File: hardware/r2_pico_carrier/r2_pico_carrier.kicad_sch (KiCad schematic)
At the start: 67 parts, among them J1 5V in, J2 OLED socket, SW1 display, U1 PCA9517A

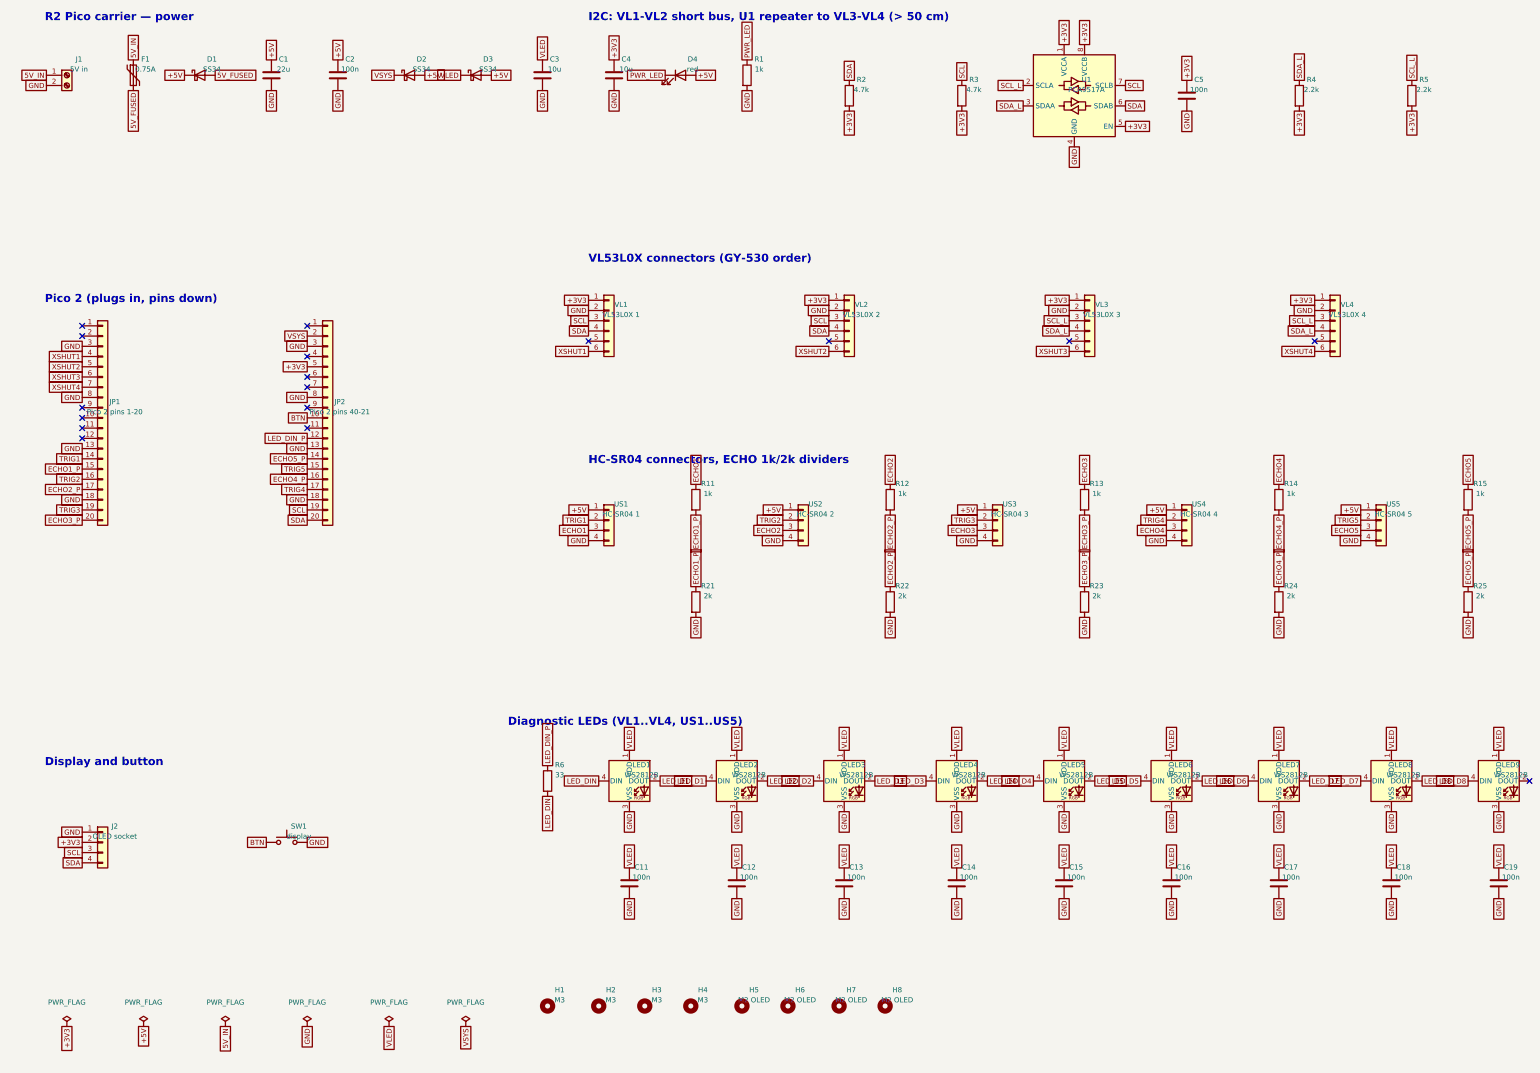
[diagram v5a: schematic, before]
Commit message: Carrier board: plain 0603 status LEDs, one GPIO each (VL1-4 = GP28/27/22/9, US1-5 = GP0/1/6-8), in place of the WS2812B chain; no VLED rail; BOM 17 lines
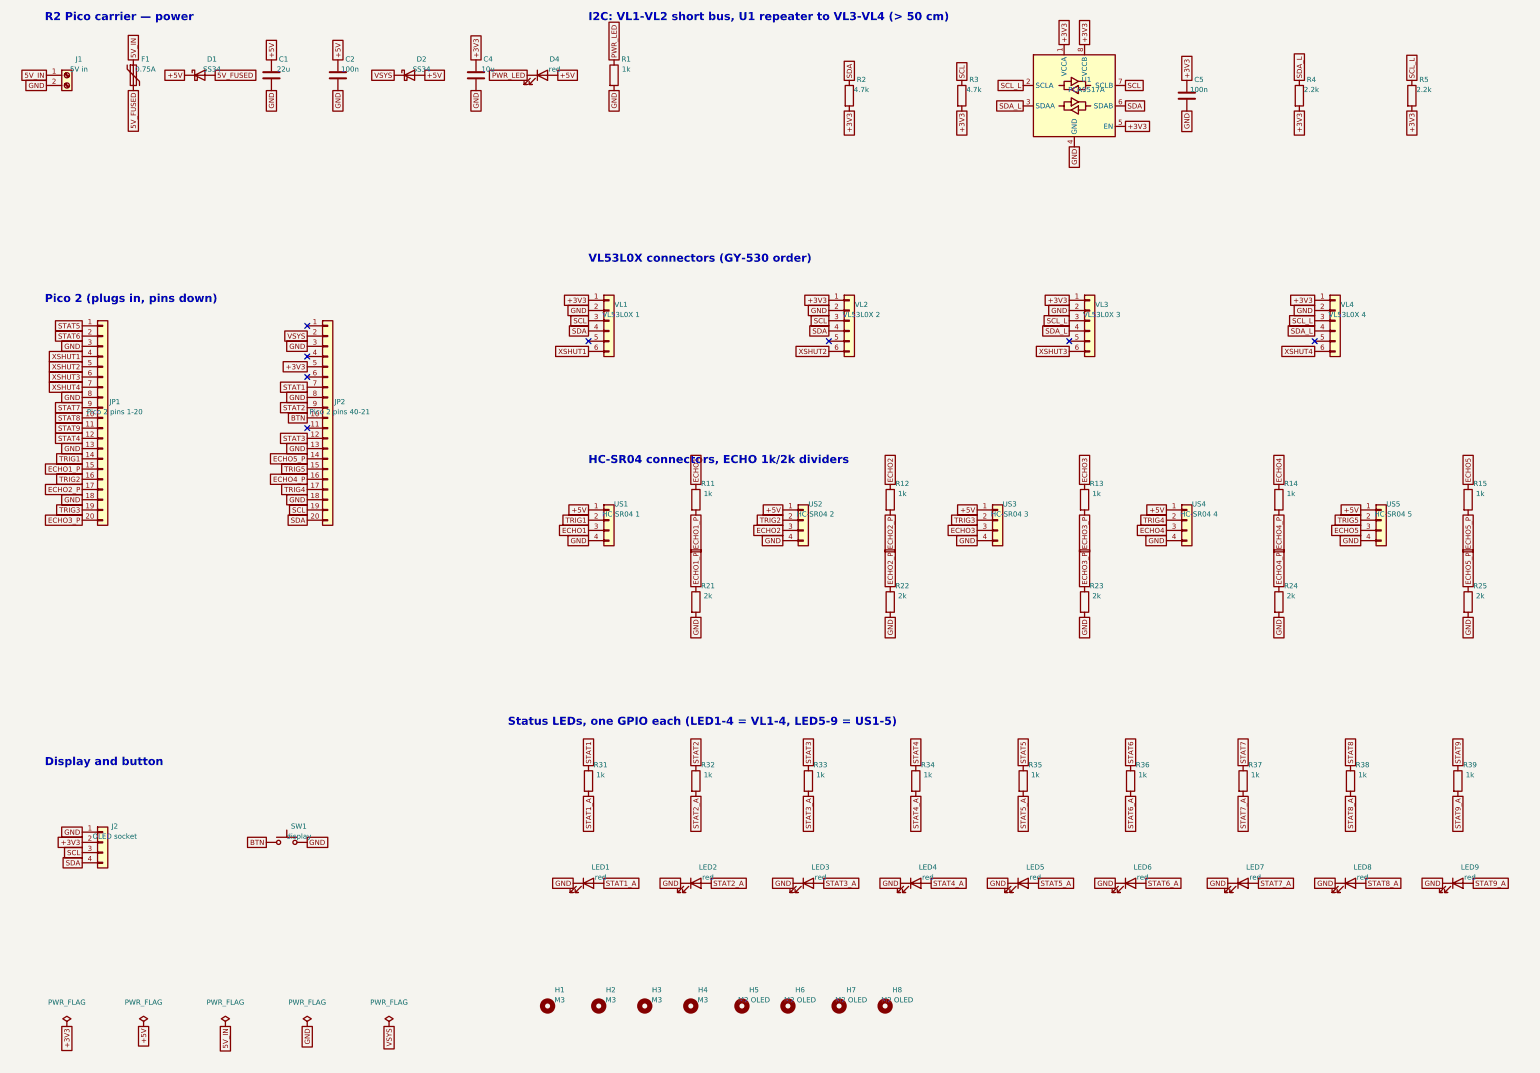
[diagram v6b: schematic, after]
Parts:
- removed C11, C12, C13, C14, C15, C16, C17, C18, C19: 100n, Capacitor_SMD:C_0603_1608Metric, symbol Device:C
- removed C3: 10u, Capacitor_SMD:C_0805_2012Metric, symbol Device:C
- removed D3: SS34, Diode_SMD:D_SMA, symbol Device:D_Schottky
- removed R6: 33, Resistor_SMD:R_0603_1608Metric, symbol Device:R
- added R31, R32, R33, R34, R35, R36, R37, R38, R39: 1k, Resistor_SMD:R_0603_1608Metric, symbol Device:R
- LED1, LED2, LED3, LED4, LED5, LED6, LED7, LED8, LED9: value WS2812B -> red; footprint LED_SMD:LED_WS2812B_PLCC4_5.0x5.0mm_P3.2mm -> LED_SMD:LED_0603_1608Metric; symbol LED:WS2812B -> Device:LED; LCSC C2874885 -> C2286
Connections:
- net VLED is gone; now on net GND: LED1.1 (K), LED2.1 (K), LED3.1 (K), LED4.1 (K), LED5.1 (K), LED6.1 (K), LED7.1 (K), LED8.1 (K), LED9.1 (K)
- net GND: no longer LED1.3 (VSS), LED2.3 (VSS), LED3.3 (VSS), LED4.3 (VSS), LED5.3 (VSS), LED6.3 (VSS), LED7.3 (VSS), LED8.3 (VSS), LED9.3 (VSS)
- net STAT9_A: now reaches LED9.2 (A)
- net STAT9_A: now also R39.2
- net STAT5: now reaches JP1.1 (Pin_1)
- net STAT5: now also R35.1
- net STAT8: now reaches JP1.10 (Pin_10)
- net STAT8: now also R38.1
- net STAT9: now reaches JP1.11 (Pin_11)
- net STAT9: now also R39.1
- net STAT4: now reaches JP1.12 (Pin_12)
- net STAT4: now also R34.1
- net STAT6: now reaches JP1.2 (Pin_2)
- net STAT6: now also R36.1
- net STAT7: now reaches JP1.9 (Pin_9)
- net STAT7: now also R37.1
- net STAT1: now reaches JP2.7 (Pin_7)
- net STAT1: now also R31.1
- net STAT2: now reaches JP2.9 (Pin_9)
- net STAT2: now also R32.1
- net LED_D1 renamed STAT1_A
- net STAT1_A: now also R31.2; no longer LED2.4 (DIN)
- net LED_D2 renamed STAT2_A
- net STAT2_A: now also R32.2; no longer LED3.4 (DIN)
- net LED_D3 renamed STAT3_A
- net STAT3_A: now also R33.2; no longer LED4.4 (DIN)
- net LED_D4 renamed STAT4_A
- net STAT4_A: now also R34.2; no longer LED5.4 (DIN)
- net LED_D5 renamed STAT5_A
- net STAT5_A: now also R35.2; no longer LED6.4 (DIN)
- net LED_D6 renamed STAT6_A
- net STAT6_A: now also R36.2; no longer LED7.4 (DIN)
- net LED_D7 renamed STAT7_A
- net STAT7_A: now also R37.2; no longer LED8.4 (DIN)
- net LED_D8 renamed STAT8_A
- net STAT8_A: now also R38.2; no longer LED9.4 (DIN)
- removed net LED_DIN: LED1.4 (DIN)
- net LED_DIN_P renamed STAT3
- net STAT3: now also R33.1
- no-connect marks 17 -> 8
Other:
- note added: "Status LEDs, one GPIO each (LED1-4 = VL1-4, LED5-9 = US1-5)"
- note removed: "Diagnostic LEDs (VL1..VL4, US1..US5)"
- moved on the sheet: C4, D4, R1

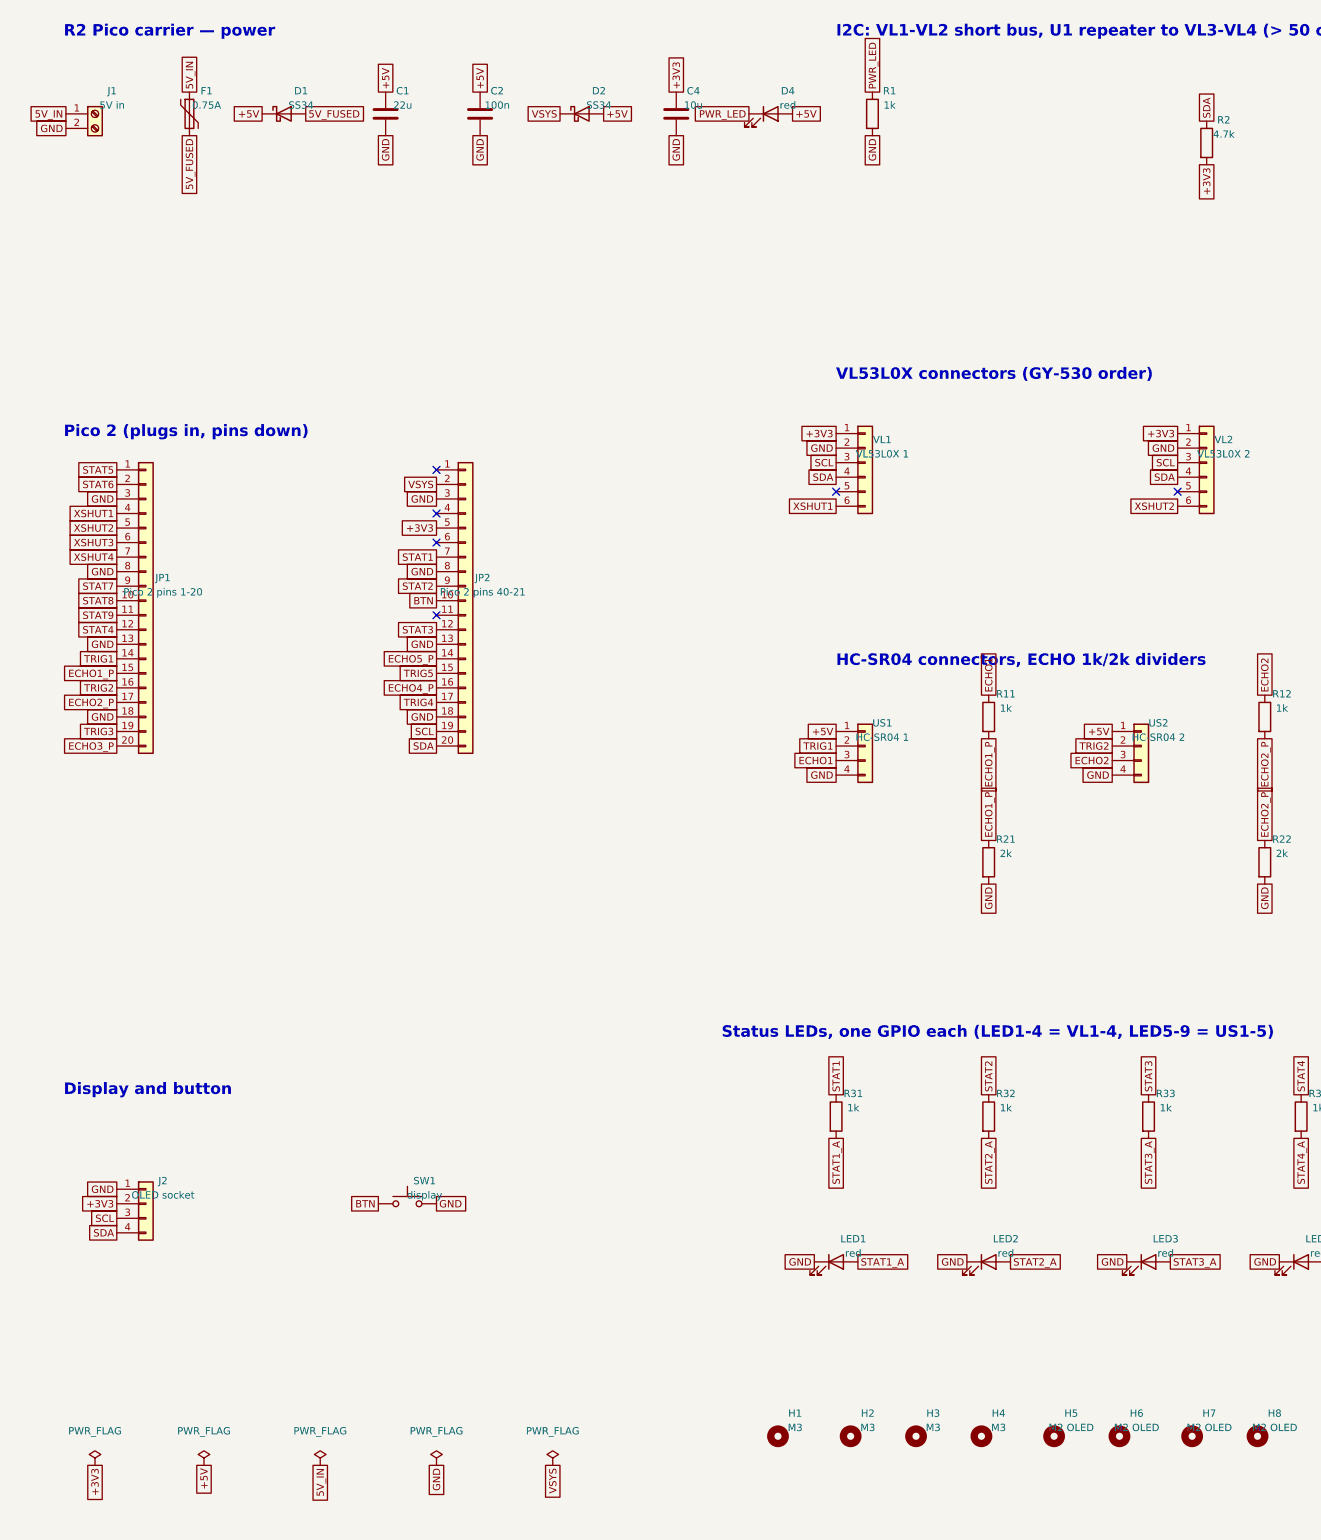
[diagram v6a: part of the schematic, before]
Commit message: Carrier board: USB-C power input (5.1k on CC, own SS34, shared fuse), Qwiic + 6-pin expansion header (I2C, 5V, 3V3, RUN), Astromech logo on the front
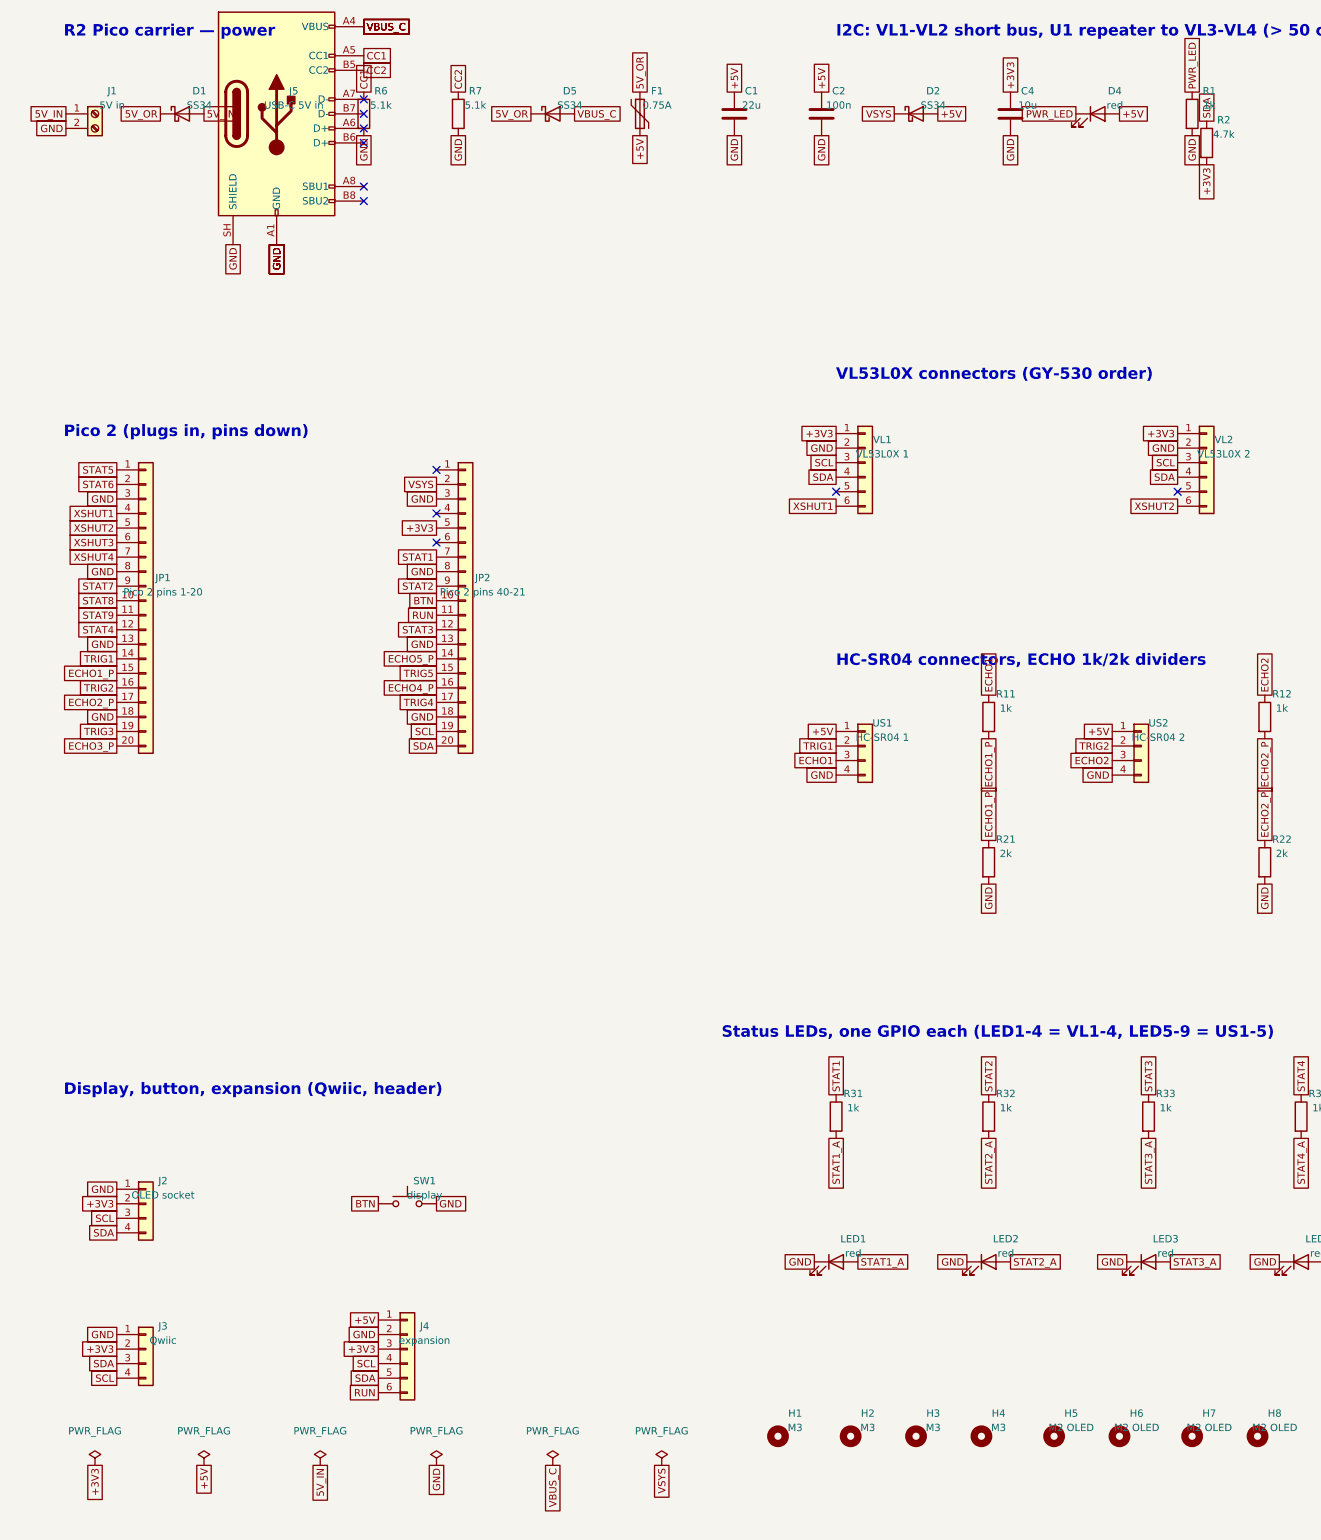
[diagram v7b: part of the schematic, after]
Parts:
- added D5: SS34, Diode_SMD:D_SMA, symbol Device:D_Schottky
- added J3: Qwiic, Connector_JST:JST_SH_BM04B-SRSS-TB_1x04-1MP_P1.00mm_Vertical, symbol Connector_Generic:Conn_01x04
- added J4: expansion, Connector_PinHeader_2.54mm:PinHeader_1x06_P2.54mm_Vertical, symbol Connector_Generic:Conn_01x06
- added J5: USB-C 5V in, Connector_USB:USB_C_Receptacle_HRO_TYPE-C-31-M-12, symbol Connector:USB_C_Receptacle_USB2.0_16P
- added R6, R7: 5.1k, Resistor_SMD:R_0603_1608Metric, symbol Device:R
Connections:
- net +3V3: now also J3.2 (Pin_2), J4.3 (Pin_3)
- net +5V: now also F1.2, J4.1 (Pin_1); no longer D1.1 (K)
- net 5V_IN: now also D1.2 (A); no longer F1.1
- net GND: now also J3.1 (Pin_1), J4.2 (Pin_2), J5.A1 (GND), J5.A12 (GND), J5.B1 (GND), J5.B12 (GND), J5.SH (SHIELD), R6.2, R7.2
- net SCL: now also J3.4 (Pin_4), J4.4 (Pin_4)
- net SDA: now also J3.3 (Pin_3), J4.5 (Pin_5)
- net RUN: now reaches JP2.11 (Pin_11)
- net RUN: now also J4.6 (Pin_6)
- removed net 5V_FUSED: D1.2 (A), F1.2
- new net 5V_OR: D1.1 (K), D5.1 (K), F1.1
- new net CC1: J5.A5 (CC1), R6.1
- new net CC2: J5.B5 (CC2), R7.1
- new net VBUS_C: D5.2 (A), J5.A4 (VBUS), J5.A9 (VBUS), J5.B4 (VBUS), J5.B9 (VBUS)
- no-connect marks 8 -> 13
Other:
- note added: "Display, button, expansion (Qwiic, header)"
- note removed: "Display and button"
- moved on the sheet: C1, C2, C4, D1, D2, D4, F1, R1
